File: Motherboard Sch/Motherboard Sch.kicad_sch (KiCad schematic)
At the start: 0 parts

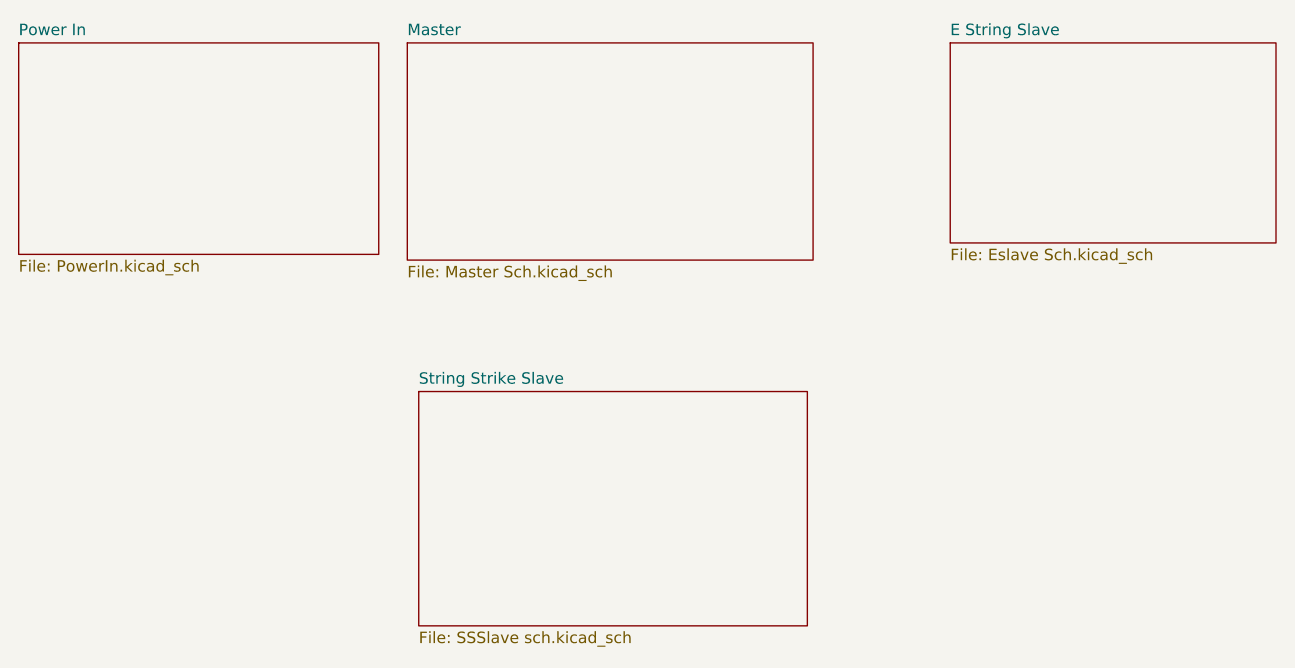
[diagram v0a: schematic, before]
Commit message: renamed Midi bass sch to Motherboard Sch
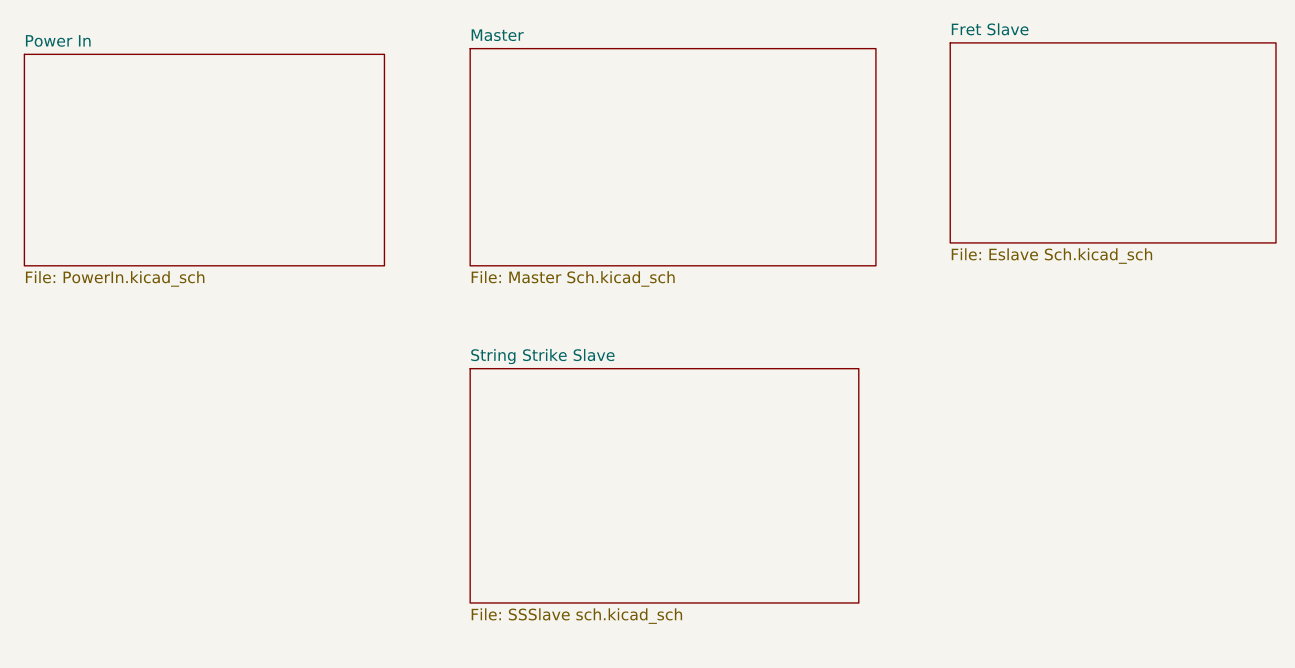
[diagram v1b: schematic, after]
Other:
- sheet E String Slave renamed Fret Slave
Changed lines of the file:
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@@
 	)
 	(sheet
-		(at 97.155 51.435)
+		(at 104.14 52.07)
 		(size 45.085 24.13)
 		(exclude_from_sim no)
@@
 		)
 		(property "Sheetname" "Master"
-			(at 97.155 50.7234 0)
+			(at 104.14 51.3584 0)
 			(effects
 				(font
@@
 		)
 		(property "Sheetfile" "Master Sch.kicad_sch"
-			(at 97.155 76.1496 0)
+			(at 104.14 76.7846 0)
 			(effects
 				(font
@@
 			(color 255 255 194 1.0000)
 		)
-		(property "Sheetname" "E String Slave"
+		(property "Sheetname" "Fret Slave"
 			(at 157.48 50.7234 0)
 			(effects
@@
 	)
 	(sheet
-		(at 98.425 90.17)
+		(at 104.14 87.63)
 		(size 43.18 26.035)
 		(exclude_from_sim no)
@@
 		)
 		(property "Sheetname" "String Strike Slave"
-			(at 98.425 89.4584 0)
+			(at 104.14 86.9184 0)
 			(effects
 				(font
@@
 		)
 		(property "Sheetfile" "SSSlave sch.kicad_sch"
-			(at 98.425 116.7896 0)
+			(at 104.14 114.2496 0)
 			(effects
 				(font
@@
 	)
 	(sheet
-		(at 53.975 51.435)
+		(at 54.61 52.705)
 		(size 40.005 23.495)
 		(exclude_from_sim no)
@@
 		)
 		(property "Sheetname" "Power In"
-			(at 53.975 50.7234 0)
+			(at 54.61 51.9934 0)
 			(effects
 				(font
@@
 		)
 		(property "Sheetfile" "PowerIn.kicad_sch"
-			(at 53.975 75.5146 0)
+			(at 54.61 76.7846 0)
 			(effects
 				(font

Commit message: updated flowcharts and names
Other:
- title: MIDI Bass Guitar Schmatic -> Bass Guitar Motherboard Sch
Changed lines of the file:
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@@
 	(paper "A")
 	(title_block
-		(title "MIDI Bass Guitar Schmatic")
+		(title "Bass Guitar Motherboard Sch")
 		(date "2024-12-10")
-		(rev "A")
+		(rev "B")
 	)
 	(sheet
@@
 		)
 		(instances
-			(project "Midi Bass Sch"
+			(project "Motherboard Sch"
 				(path "/06818073-fb22-48ee-acc5-6dedd827034e"
 					(page "2")
@@
 		)
 		(instances
-			(project "Midi Bass Sch"
+			(project "Motherboard Sch"
 				(path "/06818073-fb22-48ee-acc5-6dedd827034e"
 					(page "3")
@@
 		)
 		(instances
-			(project "Midi Bass Sch"
+			(project "Motherboard Sch"
 				(path "/06818073-fb22-48ee-acc5-6dedd827034e"
 					(page "4")
@@
 		)
 		(instances
-			(project "Midi Bass Sch"
+			(project "Motherboard Sch"
 				(path "/06818073-fb22-48ee-acc5-6dedd827034e"
 					(page "13")
